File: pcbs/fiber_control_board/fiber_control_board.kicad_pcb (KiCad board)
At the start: 2 copper layers, 119.5 x 139 mm, 59 parts, among them J1 2.1x5.5mm_9V, J2 Trig_BNC, J3 AFBR-2624Z Trig_I, J4 AFBR-1624Z Trig_O, J5 Clk_BNC, J6 AFBR-1624Z Clk_O, J7 AFBR-2624Z Clk_I, J8 AFBR-1624Z En_O, SW1 SW_DPDT_x2, SW2 SW_Push_SPDT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

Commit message: Added some silkscreen to the fiber control board
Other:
- board text added: "2.1x5.5mm 9V"
- board text added: "Clock In"
- board text added: "Trigger In"
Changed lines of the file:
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@@
 			(layer "F.SilkS")
 		)
+		(fp_line
+			(start -0.225 1.975)
+			(end -0.575 1.975)
+			(stroke
+				(width 0.1)
+				(type default)
+			)
+			(layer "F.SilkS")
+		)
 		(fp_circle
 			(center 0 1.5)
@@
 		(layer "Edge.Cuts")
 	)
+	(gr_text "Trigger\nIn"
+		(at 60 144 0)
+		(layer "F.SilkS")
+		(effects
+			(font
+				(size 1.5 1.5)
+				(thickness 0.3)
+				(bold yes)
+			)
+		)
+	)
+	(gr_text "2.1x5.5mm\n9V"
+		(at 67 49 0)
+		(layer "F.SilkS")
+		(effects
+			(font
+				(size 1.5 1.5)
+				(thickness 0.3)
+				(bold yes)
+			)
+		)
+	)
 	(gr_text "Enable\nOut"
 		(at 152.2 64.5 0)
@@
 		)
 	)
+	(gr_text "Clock\nIn\n"
+		(at 60 84 0)
+		(layer "F.SilkS")
+		(effects
+			(font
+				(size 1.5 1.5)
+				(thickness 0.3)
+				(bold yes)
+			)
+		)
+	)
 	(gr_text "Clock\nOut"
 		(at 142 64.5 0)
@@
 	)
 	(group ""
-		(members "462b457e-6405-4e14-b1d3-06a891a581de" "78cb7611-1a67-4fdc-b7c8-a2074ca4b056"
+		(members "330c18c2-d340-46d3-9040-301c8e4d5157" "462b457e-6405-4e14-b1d3-06a891a581de"
+			"4ac1904f-517d-44d8-936b-ae50fc5a540d" "78cb7611-1a67-4fdc-b7c8-a2074ca4b056"
 			"89eed348-e99f-434b-a4a7-9268c5d69a36" "948f8894-4a2a-4598-9eeb-570c1488be8a"
-			"e014415c-c803-4f65-84e5-522754b20bce" "f3a178c4-98d2-4d0c-8edb-dfd8b7053ac0"
+			"98fb0666-7d6f-4912-be88-05ddaef28902" "e014415c-c803-4f65-84e5-522754b20bce"
+			"f3a178c4-98d2-4d0c-8edb-dfd8b7053ac0"
 		)
 	)

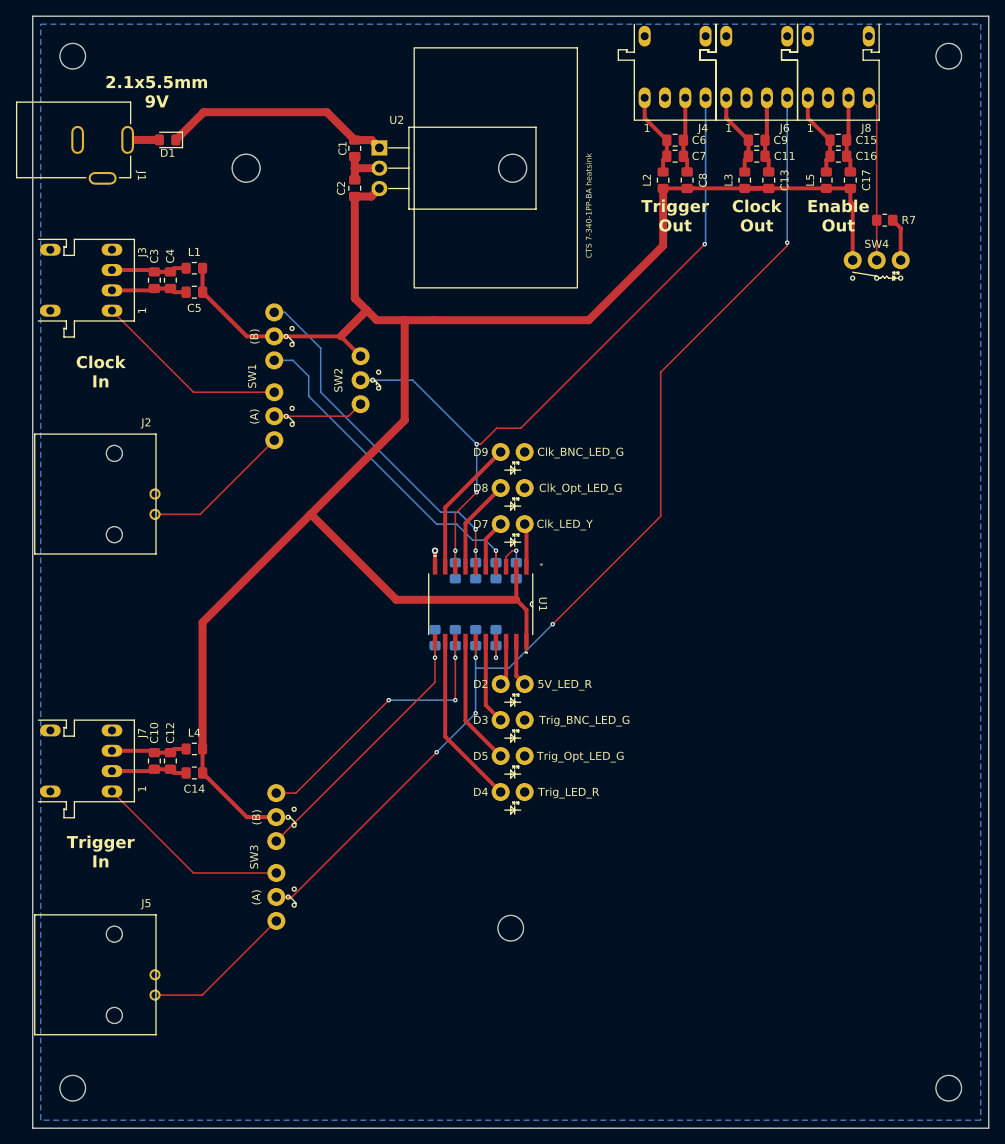
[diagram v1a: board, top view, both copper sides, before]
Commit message: Tweaked serial interface and fiber control boards. Added empty manufacturing folder to indicate where to dump gerbers
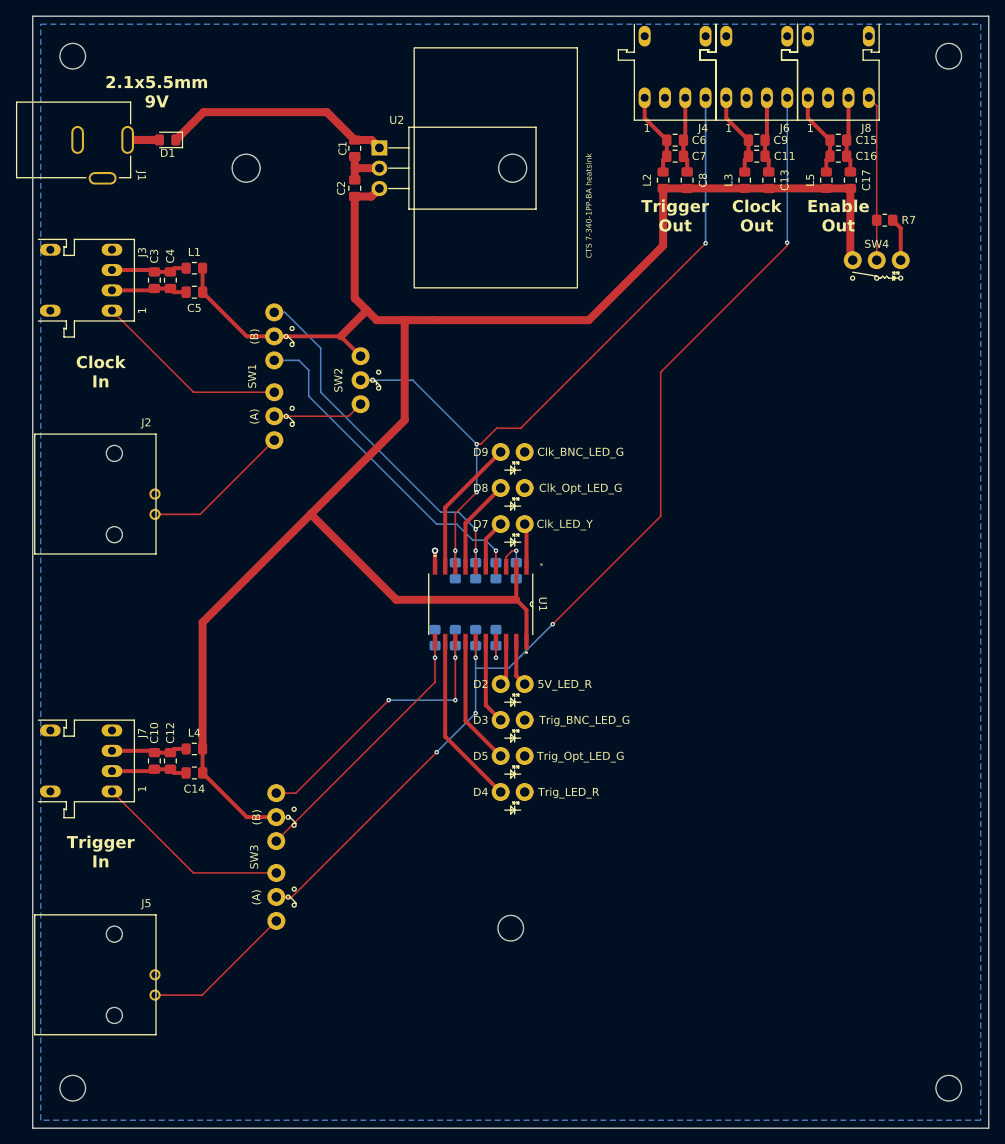
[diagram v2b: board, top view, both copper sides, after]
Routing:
- net +5V: track 251.7 -> 249.4 mm
- net /Clock/Clk_LED: track 136.7 -> 134.7 mm
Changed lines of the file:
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@@
-	)
-	(segment
-		(start 154 63)
-		(end 154 70)
-		(width 0.5)
-		(layer "F.Cu")
-		(net 3)
 	)
 	(segment
@@
 	)
 	(segment
+		(start 130.3 61.025)
+		(end 153.6875 61.025)
+		(width 1)
+		(layer "F.Cu")
+		(net 3)
+	)
+	(segment
 		(start 93.830308 62.042494)
 		(end 94.832802 61.04)
@@
 	)
 	(segment
-		(start 140.5 61.025)
-		(end 143.4875 61.025)
-		(width 0.5)
+		(start 153.6875 61.025)
+		(end 153.7 61.0375)
+		(width 1)
 		(layer "F.Cu")
 		(net 3)
@@
 	)
 	(segment
-		(start 153.7 62.7)
-		(end 154 63)
-		(width 0.5)
-		(layer "F.Cu")
-		(net 3)
-	)
-	(segment
 		(start 72.73 115.27)
 		(end 72.73 131.095)
@@
 	)
 	(segment
+		(start 153.7 69.7)
+		(end 154 70)
+		(width 1)
+		(layer "F.Cu")
+		(net 3)
+	)
+	(segment
 		(start 91.751665 74.751665)
 		(end 93.25 76.25)
@@
 	)
 	(segment
-		(start 153.7 61.0375)
-		(end 153.7 62.7)
-		(width 0.5)
-		(layer "F.Cu")
-		(net 3)
-	)
-	(segment
-		(start 133.975 61.025)
-		(end 150.7 61.025)
-		(width 0.5)
-		(layer "F.Cu")
-		(net 3)
-	)
-	(segment
 		(start 72.7425 74)
 		(end 78.262945 79.520445)
@@
 	)
 	(segment
-		(start 150.7 61.025)
-		(end 153.6875 61.025)
-		(width 0.5)
+		(start 153.7 61.0375)
+		(end 153.7 69.7)
+		(width 1)
 		(layer "F.Cu")
 		(net 3)
@@
 	)
 	(segment
-		(start 153.6875 61.025)
-		(end 153.7 61.0375)
-		(width 0.5)
-		(layer "F.Cu")
-		(net 3)
-	)
-	(segment
 		(start 101.5 77.5)
 		(end 121 77.5)
@@
 	)
 	(segment
-		(start 130.3 61.025)
-		(end 133.2875 61.025)
-		(width 0.5)
-		(layer "F.Cu")
-		(net 3)
-	)
-	(segment
 		(start 66.4725 71.23)
 		(end 66.705 71.4625)
@@
 	)
 	(segment
-		(start 81.951121 149.595)
-		(end 83.905 149.595)
-		(width 0.2)
-		(layer "B.Cu")
-		(net 22)
-	)
-	(segment
 		(start 111 121)
 		(end 112.5 119.5)
@@
 	)
 	(segment
-		(start 84.020445 82.520445)
-		(end 86 84.5)
+		(start 81.685709 82.520445)
+		(end 84.770445 82.520445)
+		(width 0.2)
+		(layer "B.Cu")
+		(net 33)
+	)
+	(segment
+		(start 108.0913 105)
+		(end 109.405 106.3137)
+		(width 0.2)
+		(layer "B.Cu")
+		(net 33)
+	)
+	(segment
+		(start 102 103)
+		(end 104.5 103)
+		(width 0.2)
+		(layer "B.Cu")
+		(net 33)
+	)
+	(segment
+		(start 84.770445 82.520445)
+		(end 86 83.75)
+		(width 0.2)
+		(layer "B.Cu")
+		(net 33)
+	)
+	(segment
+		(start 86 83.75)
+		(end 86 87)
+		(width 0.2)
+		(layer "B.Cu")
+		(net 33)
+	)
+	(segment
+		(start 109.405 107.8137)
+		(end 109.405 106.3137)
+		(width 0.2)
+		(layer "B.Cu")
+		(net 33)
+	)
+	(segment
+		(start 106.5 105)
+		(end 108.0913 105)
 		(width 0.2)
 		(layer "B.Cu")
@@
 	)
 	(segment
-		(start 81.685709 82.520445)
-		(end 84.020445 82.520445)
-		(width 0.2)
-		(layer "B.Cu")
-		(net 33)
-	)
-	(segment
-		(start 106.5 105)
-		(end 108.0913 105)
-		(width 0.2)
-		(layer "B.Cu")
-		(net 33)
-	)
-	(segment
-		(start 109.405 107.8137)
-		(end 109.405 106.3137)
-		(width 0.2)
-		(layer "B.Cu")
-		(net 33)
-	)
-	(segment
-		(start 86 84.5)
-		(end 86 87)
-		(width 0.2)
-		(layer "B.Cu")
-		(net 33)
-	)
-	(segment
-		(start 102 103)
-		(end 104.5 103)
-		(width 0.2)
-		(layer "B.Cu")
-		(net 33)
-	)
-	(segment
-		(start 108.0913 105)
-		(end 109.405 106.3137)
-		(width 0.2)
-		(layer "B.Cu")
-		(net 33)
-	)
-	(segment
 		(start 86 87)
 		(end 102 103)
@@
 	)
 	(segment
+		(start 135.61 67.89)
+		(end 112.5 91)
+		(width 0.2)
+		(layer "F.Cu")
+		(net 34)
+	)
+	(segment
+		(start 112.5 91)
+		(end 109.5 91)
+		(width 0.2)
+		(layer "F.Cu")
+		(net 34)
+	)
+	(segment
 		(start 107 99)
 		(end 104.325 101.675)
@@
 	)
 	(segment
-		(start 109.5 91)
-		(end 112.5 91)
-		(width 0.2)
-		(layer "F.Cu")
-		(net 34)
-	)
-	(segment
-		(start 112.5 91)
-		(end 135.5 68)
+		(start 107.5 93)
+		(end 107 93)
 		(width 0.2)
 		(layer "F.Cu")
@@
 	)
 	(segment
-		(start 135.5 68)
-		(end 135.61 67.89)
-		(width 0.2)
-		(layer "F.Cu")
-		(net 34)
-	)
-	(segment
-		(start 107 93)
+		(start 109.5 91)
 		(end 107.5 93)
 		(width 0.2)
@@
 		(net 34)
 	)
-	(segment
-		(start 107.5 93)
-		(end 109.5 91)
-		(width 0.2)
-		(layer "F.Cu")
-		(net 34)
-	)
-	(via
-		(at 135.5 68)
+	(via
+		(at 135.61 67.89)
 		(size 0.56)
 		(drill 0.254)
@@
 			"41c52b45-6415-4396-bdc6-f124ea98c8e1" "44e81b36-61d4-4ebd-afc1-8f58230e6b2b"
 			"5effa987-7035-4673-87bb-ec7487b018c8" "67d1b0ec-b9cc-4ef6-bccf-82df7faf59e4"
-			"6bd30a2a-ee1c-4b44-a498-d49223622270" "786fedbb-166b-4e9c-8919-5bf51e829659"
-			"9293a5cc-f4fe-40c3-b339-a517a0d6be37" "96b2c0af-cc18-4e32-9202-02eca0672459"
-			"96c1c6e1-8ca0-4a56-9100-7cd630645932" "d541a783-d78a-41dc-ad5d-5b9942b19624"
-			"ff14a9bb-c9ff-47b1-954f-c2f00972bfb4"
+			"786fedbb-166b-4e9c-8919-5bf51e829659" "9293a5cc-f4fe-40c3-b339-a517a0d6be37"
+			"96b2c0af-cc18-4e32-9202-02eca0672459" "96c1c6e1-8ca0-4a56-9100-7cd630645932"
+			"d541a783-d78a-41dc-ad5d-5b9942b19624" "ff14a9bb-c9ff-47b1-954f-c2f00972bfb4"
 		)
 	)
@@
 	(group ""
 		(members "233894a5-57da-40d0-a241-d1bef8d6f80f" "2731ce0c-61d4-43d8-a874-18bade3502ab"
-			"345f6edd-ba32-48eb-b8d2-b509c0e89810" "705c04d8-d491-4b53-97ca-a09dce3e04a9"
+			"343c6793-7ff9-4ee6-a952-053459d451a8" "345f6edd-ba32-48eb-b8d2-b509c0e89810"
+			"624e00ce-f296-418f-80d5-da7e9a7fa99b" "705c04d8-d491-4b53-97ca-a09dce3e04a9"
 			"726ba5ce-a950-4452-827b-8ea95db14283" "8061dd72-5d38-4548-9964-8d3421b8f7b2"
 			"868bf2ff-432e-4c06-93b3-bcbf66ac703b" "8fddaf89-a33a-4814-a1f7-212689eef5b1"
 			"c2290989-8b6a-4c55-9756-008358ce5085" "cb9fc583-89ac-4119-9045-cd273b52bbf1"
-			"d7c0d632-8d5f-4dae-8ffc-59c1f8806e2d" "db421301-7baa-46b7-8985-ac21b2a01ff4"
-			"f49a0ea6-e294-4377-84df-22609e8b812e"
+			"d7c0d632-8d5f-4dae-8ffc-59c1f8806e2d"
 		)
 	)
@@
 			"a643b131-9139-47a3-a534-5a9646c1d503" "e3bb379b-b8ae-4525-95d0-0cfd41acf3f8"
 			"e742b536-5e44-439a-af84-8d16efb1125d" "eda21316-0bc9-4ca7-ac27-4110f71cf2b9"
-			"ff27c90e-629e-47f3-bba0-038cc51f7d34"
 		)
 	)
@@
 	)
 	(group ""
-		(members "00a51d72-bf22-4710-9e82-f4fe966d5976" "0eaf5815-f099-4221-b799-b11fbd773242"
-			"1bb86e2b-5bbe-4f7c-bd08-b727c9053f88" "1fcafb75-ca95-4bf9-bc48-a2aaeffb2de6"
-			"334bc7ae-2ad0-4635-9c68-a5c941cf04b5" "93e4e840-8440-46b3-a704-baefb5d3ac0e"
-			"a8154e14-f63a-421a-9a8c-daa78ebd8577" "be85f9bd-cfb7-4262-ab69-2d45178b80a3"
-			"eb556568-42fd-4532-8509-02aa32e0ecbd" "ff226962-8b69-4b2e-8cf2-3b9694c6ee27"
-		)
-	)
+		(members "00a51d72-bf22-4710-9e82-f4fe966d5976" "1bb86e2b-5bbe-4f7c-bd08-b727c9053f88"
+			"1fcafb75-ca95-4bf9-bc48-a2aaeffb2de6" "334bc7ae-2ad0-4635-9c68-a5c941cf04b5"
+			"9f0f5159-f26c-4704-baff-fab02723af6b" "be85f9bd-cfb7-4262-ab69-2d45178b80a3"
+			"ddc5fbba-c845-453e-99fa-da0d2da2f5b7" "eb556568-42fd-4532-8509-02aa32e0ecbd"
+			"ff226962-8b69-4b2e-8cf2-3b9694c6ee27"
+		)
+	)
